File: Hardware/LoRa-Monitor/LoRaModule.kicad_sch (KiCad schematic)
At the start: 3 parts, among them U15 E22-900M30S

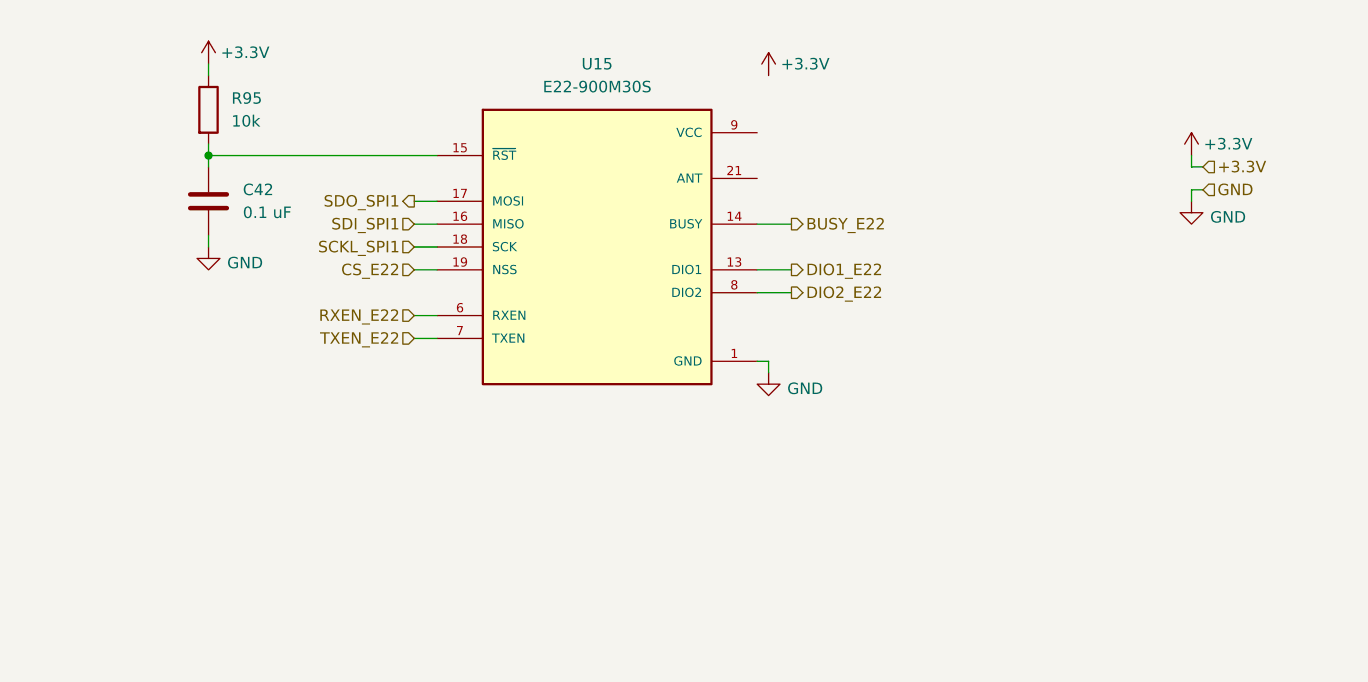
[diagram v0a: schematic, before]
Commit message: Finished MCU and Lora modules. Finished Connectors sheet
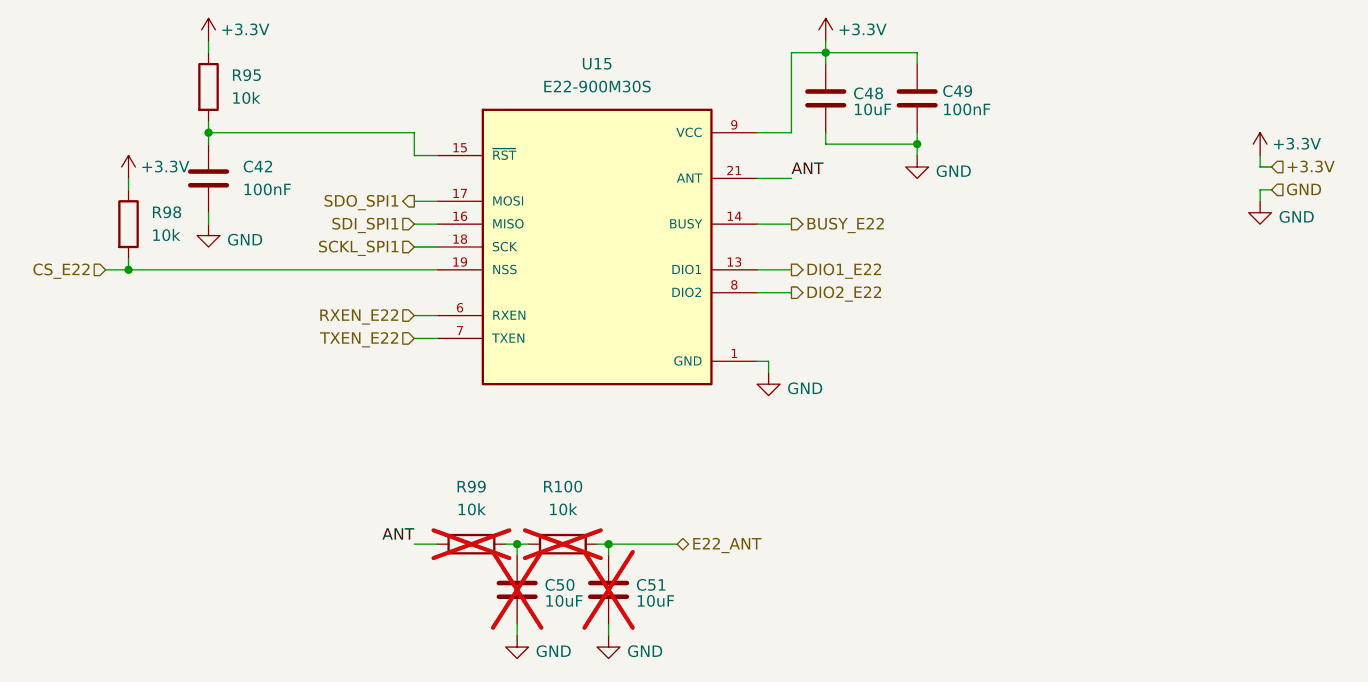
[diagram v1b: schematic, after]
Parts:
- added C48, C50, C51: 10uF, Capacitor_SMD:C_0805_2012Metric, symbol Device:C
- added C49: 100nF, Capacitor_SMD:C_0805_2012Metric, symbol Device:C
- added R100, R98, R99: 10k, Resistor_SMD:R_0805_2012Metric, symbol Device:R
- C42: value 0.1 uF -> 100nF
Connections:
- net VCC is gone; now on net +3.3V: U15.10 (VCC), U15.9 (VCC)
- net +3.3V: now also C48.1, C49.1, R98.1
- net CS_E22: now also R98.2
- net GND: now also C48.2, C49.2, C50.2, C51.2
- net ANT: now reaches U15.21 (ANT)
- net ANT: now also R99.1
- new net: C50.1, R100.1, R99.2
- new net E22_ANT: C51.1, R100.2
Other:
- moved on the sheet: C42, R95

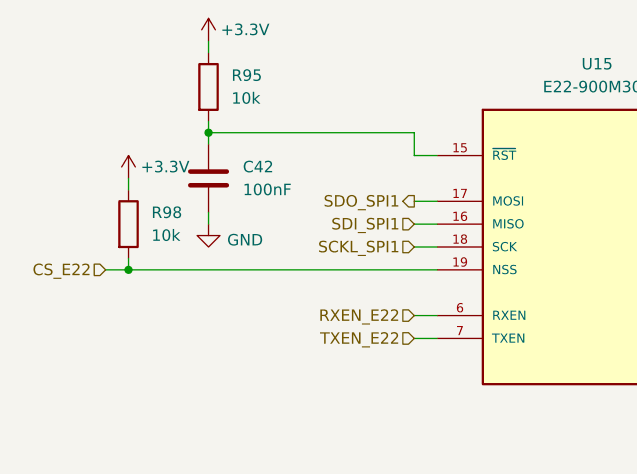
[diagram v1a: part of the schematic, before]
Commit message: Finished schematic, started with PCB design
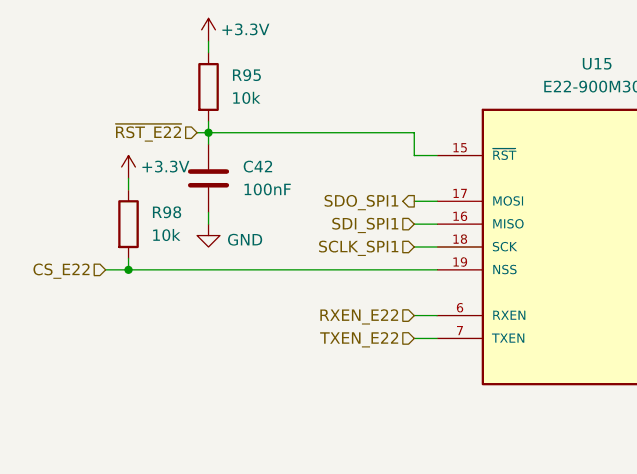
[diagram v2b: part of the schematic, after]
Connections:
- net ~{RST_E22}: now reaches C42.1, R95.2, U15.15 (~{RST})
- net SCKL_SPI1 renamed SCLK_SPI1
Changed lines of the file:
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@@
+	(wire
+		(pts
+			(xy 92.71 73.66) (xy 93.98 73.66)
+		)
+		(stroke
+			(width 0)
+			(type default)
+		)
+	)
 	(wire
 		(pts
@@
 		)
 	)
+	(hierarchical_label "SCLK_SPI1"
+		(shape input)
+		(at 116.84 86.36 180)
+		(effects
+			(font
+				(size 1.27 1.27)
+			)
+			(justify right)
+		)
+	)
 	(hierarchical_label "CS_E22"
 		(shape input)
@@
 		)
 	)
+	(hierarchical_label "~{RST_E22}"
+		(shape input)
+		(at 92.71 73.66 180)
+		(effects
+			(font
+				(size 1.27 1.27)
+			)
+			(justify right)
+		)
+	)
 	(hierarchical_label "+3.3V"
 		(shape input)
@@
 		)
 	)
-	(hierarchical_label "SCKL_SPI1"
-		(shape input)
-		(at 116.84 86.36 180)
-		(effects
-			(font
-				(size 1.27 1.27)
-			)
-			(justify right)
-		)
-	)
